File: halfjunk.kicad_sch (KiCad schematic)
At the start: 94 parts, among them SW0 SW_Push, U0 ATmega32U4-A

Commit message: A lot of progress on schematic
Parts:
- removed C?: 10uf, symbol Device:C_Small
- removed C? (x3): .1uF, symbol Device:C_Small
- removed D? (x40): D_Small, symbol Device:D_Small
- removed SW? (x40): SW_Push, symbol Switch:SW_Push
- added C? (x3): .1uF, symbol Device:C_Small
- added C?: 10uf, symbol Device:C_Small
- added D? (x45): D_Small, symbol Device:D_Small
- added D?: PRTR5V0U2X, Package_TO_SOT_SMD:SOT-143, symbol Power_Protection:PRTR5V0U2X
- added F?: 500m, symbol Device:Polyfuse_Small
- added J?: AVR-ISP-6, symbol Connector:AVR-ISP-6
- added J? (x2): USB_C_Receptacle_USB2.0, symbol Connector:USB_C_Receptacle_USB2.0
- added R? (x2): 5.1k, symbol Device:R_Small
- added R? (x2): 4.7K, symbol Device:R_Small
- added SW? (x45): SW_Push, symbol Switch:SW_Push
- added SW?: RotaryEncoder, symbol Device:RotaryEncoder
- R?: value R_Small -> 10k
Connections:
- net +5V: now also C?.1, C?.1, C?.1, C?.1, F?.2, J?.2 (VCC), J?.A4 (VBUS), J?.A9 (VBUS), J?.B4 (VBUS), J?.B9 (VBUS)
- net D+: now also D?.2 (I/O1), J?.A6 (D+), J?.B6 (D+)
- net D-: now also D?.3 (I/O2), J?.A7 (D-), J?.B7 (D-)
- net GND: now also C?.2, C?.2, C?.2, C?.2, D?.1 (GND), J?.6 (GND), J?.A1 (GND), J?.A1 (GND), J?.A12 (GND), J?.A12 (GND), J?.B1 (GND), J?.B1 (GND), J?.B12 (GND), J?.B12 (GND), J?.S1 (SHIELD), J?.S1 (SHIELD), R?.2, R?.2, SW?.C
- net RST: now reaches R?.2, SW0.2, U0.13 (~{RESET})
- net RST: now also J?.5 (~{RST})
- net MOSI: now reaches U0.10 (PB2)
- net MOSI: now also J?.4 (MOSI)
- net MISO: now reaches U0.11 (PB3)
- net MISO: now also J?.1 (MISO)
- net ENC_A: now reaches U0.18 (PD0)
- net ENC_A: now also SW?.A
- net ENC_B: now reaches U0.19 (PD1)
- net ENC_B: now also SW?.B
- net at U0.20 (PD2): now also R?.1
- net at U0.21 (PD3): now also R?.1
- net ROW_0: now reaches U0.22 (PD5)
- net ROW_0: now also D?.1 (K), D?.1 (K), D?.1 (K), D?.1 (K), D?.1 (K), D?.1 (K), D?.1 (K)
- net ROW_1: now reaches U0.25 (PD4)
- net ROW_1: now also D?.1 (K), D?.1 (K), D?.1 (K), D?.1 (K), D?.1 (K), D?.1 (K), D?.1 (K)
- net ROW_2: now reaches U0.26 (PD6)
- net ROW_2: now also D?.1 (K), D?.1 (K), D?.1 (K), D?.1 (K), D?.1 (K), D?.1 (K), D?.1 (K)
- net ROW_3: now reaches U0.27 (PD7)
- net ROW_3: now also D?.1 (K), D?.1 (K), D?.1 (K), D?.1 (K), D?.1 (K), D?.1 (K), D?.1 (K)
- net ROW_4: now reaches U0.28 (PB4)
- net ROW_4: now also D?.1 (K), D?.1 (K), D?.1 (K), D?.1 (K), D?.1 (K), D?.1 (K), D?.1 (K)
- net ROW_5: now reaches U0.29 (PB5)
- net ROW_5: now also D?.1 (K), D?.1 (K), D?.1 (K), D?.1 (K), D?.1 (K)
- net ROW_6: now reaches U0.30 (PB6)
- net ROW_6: now also D?.1 (K), D?.1 (K), D?.1 (K), D?.1 (K), D?.1 (K)
- net COL_5: now reaches U0.36 (PF7)
- net COL_5: now also SW?.2, SW?.2, SW?.2, SW?.2, SW?.2, SW?.2, SW?.2
- net COL_4: now reaches U0.37 (PF6)
- net COL_4: now also SW?.2, SW?.2, SW?.2, SW?.2, SW?.2, SW?.2, SW?.2
- net COL_3: now reaches U0.38 (PF5)
- net COL_3: now also SW?.2, SW?.2, SW?.2, SW?.2, SW?.2, SW?.2, SW?.2
- net COL_2: now reaches U0.39 (PF4)
- net COL_2: now also SW?.2, SW?.2, SW?.2, SW?.2, SW?.2, SW?.2, SW?.2
- net COL_1: now reaches U0.40 (PF1)
- net COL_1: now also SW?.2, SW?.2, SW?.2, SW?.2, SW?.2
- net COL_0: now reaches U0.41 (PF0)
- net COL_0: now also SW?.2, SW?.2, SW?.2, SW?.2, SW?.2
- net SCLK: now reaches U0.9 (PB1)
- net SCLK: now also J?.3 (SCK)
- new net: D?.2 (A), SW?.1 (x45)
- new net: J?.B5 (CC2), R?.1
- new net: J?.A5 (CC1), R?.1
- new net COL_6: SW?.2, SW?.2, SW?.2, SW?.2, SW?.2, SW?.2, SW?.2
- new net DATA_1: J?.A7 (D-), J?.B7 (D-), R?.2
- new net DATA_2: J?.A6 (D+), J?.B6 (D+), R?.2
- new net VCC: D?.4 (VCC), F?.1, J?.A4 (VBUS), J?.A9 (VBUS), J?.B4 (VBUS), J?.B9 (VBUS)
- no-connect marks 0 -> 3
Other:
- note added: "Decoupling Capacitors"
- note added: "ISP"
- note added: "MCU"
- note added: "Scroll Drum"
- note added: "USB-C PC"
- moved on the sheet: C?, R?, SW0, U0, Y?

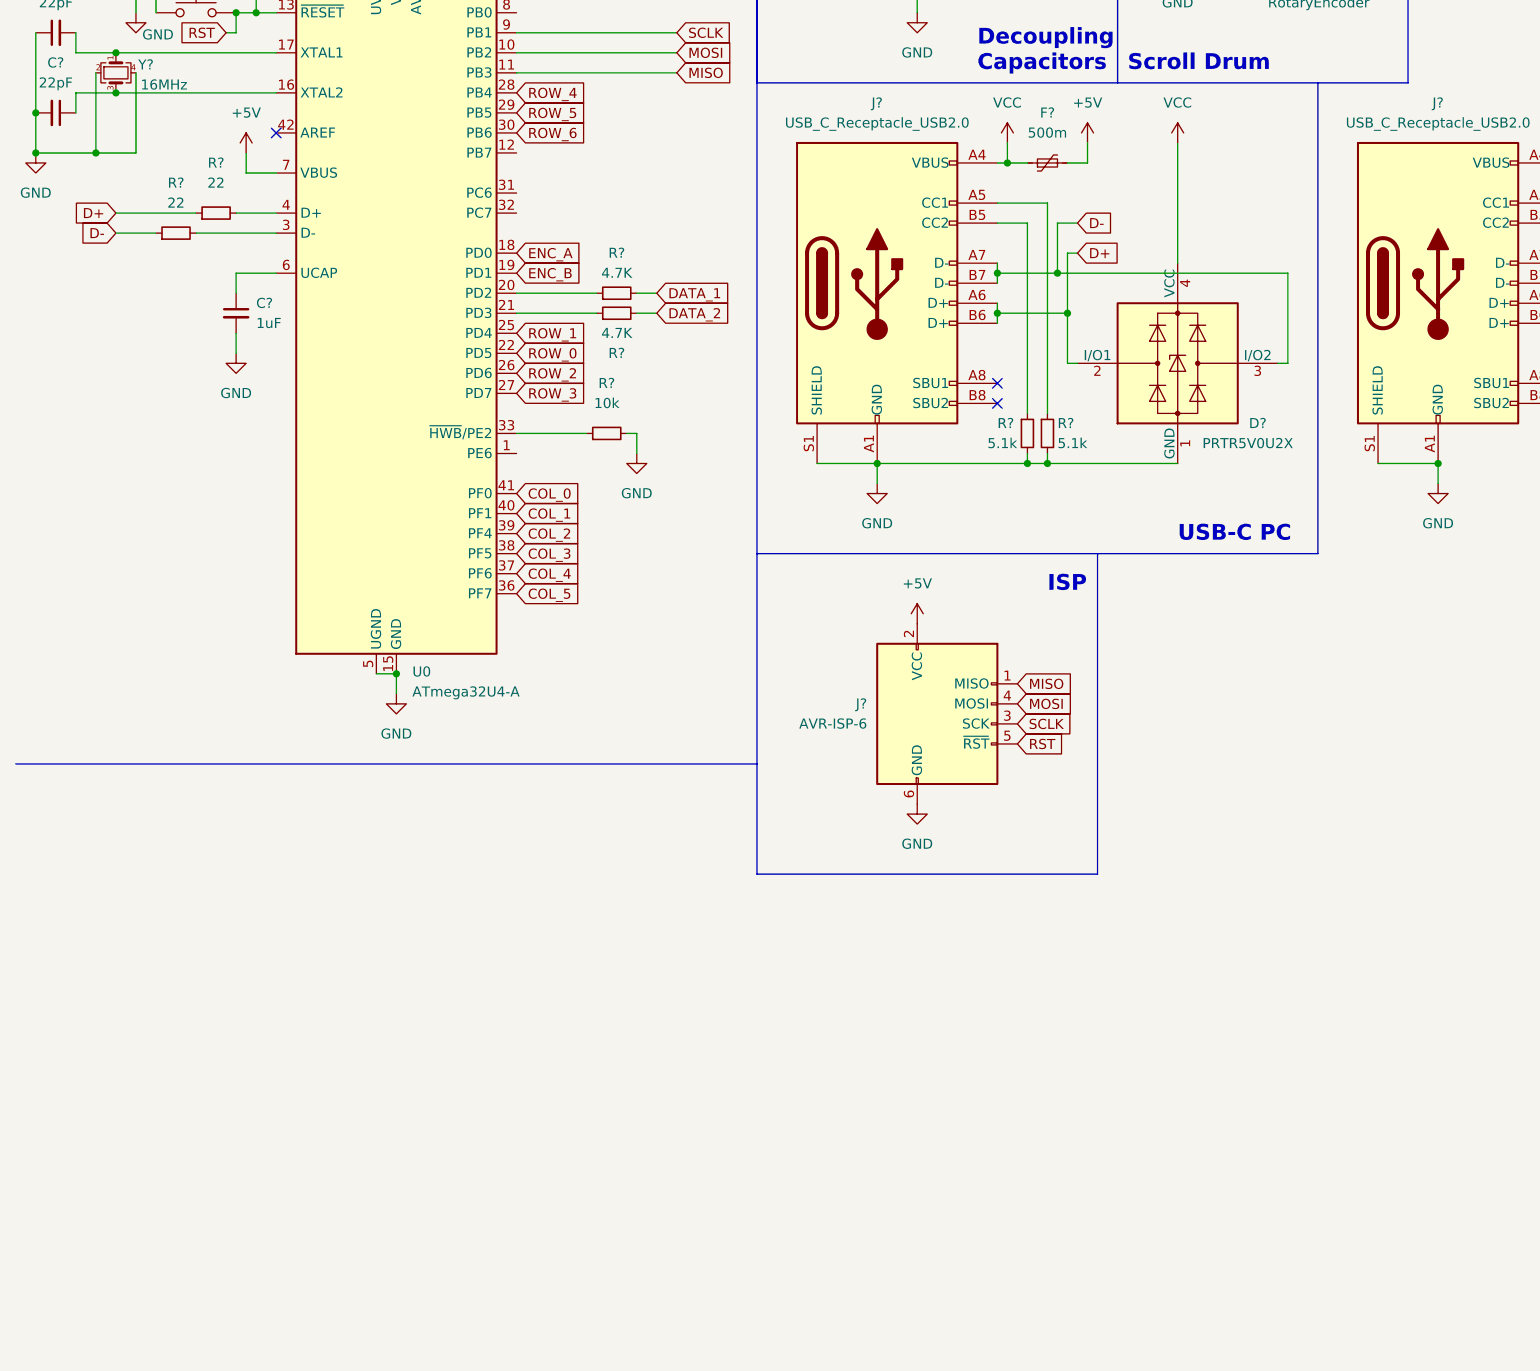
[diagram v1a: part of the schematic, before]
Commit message: added LEDs
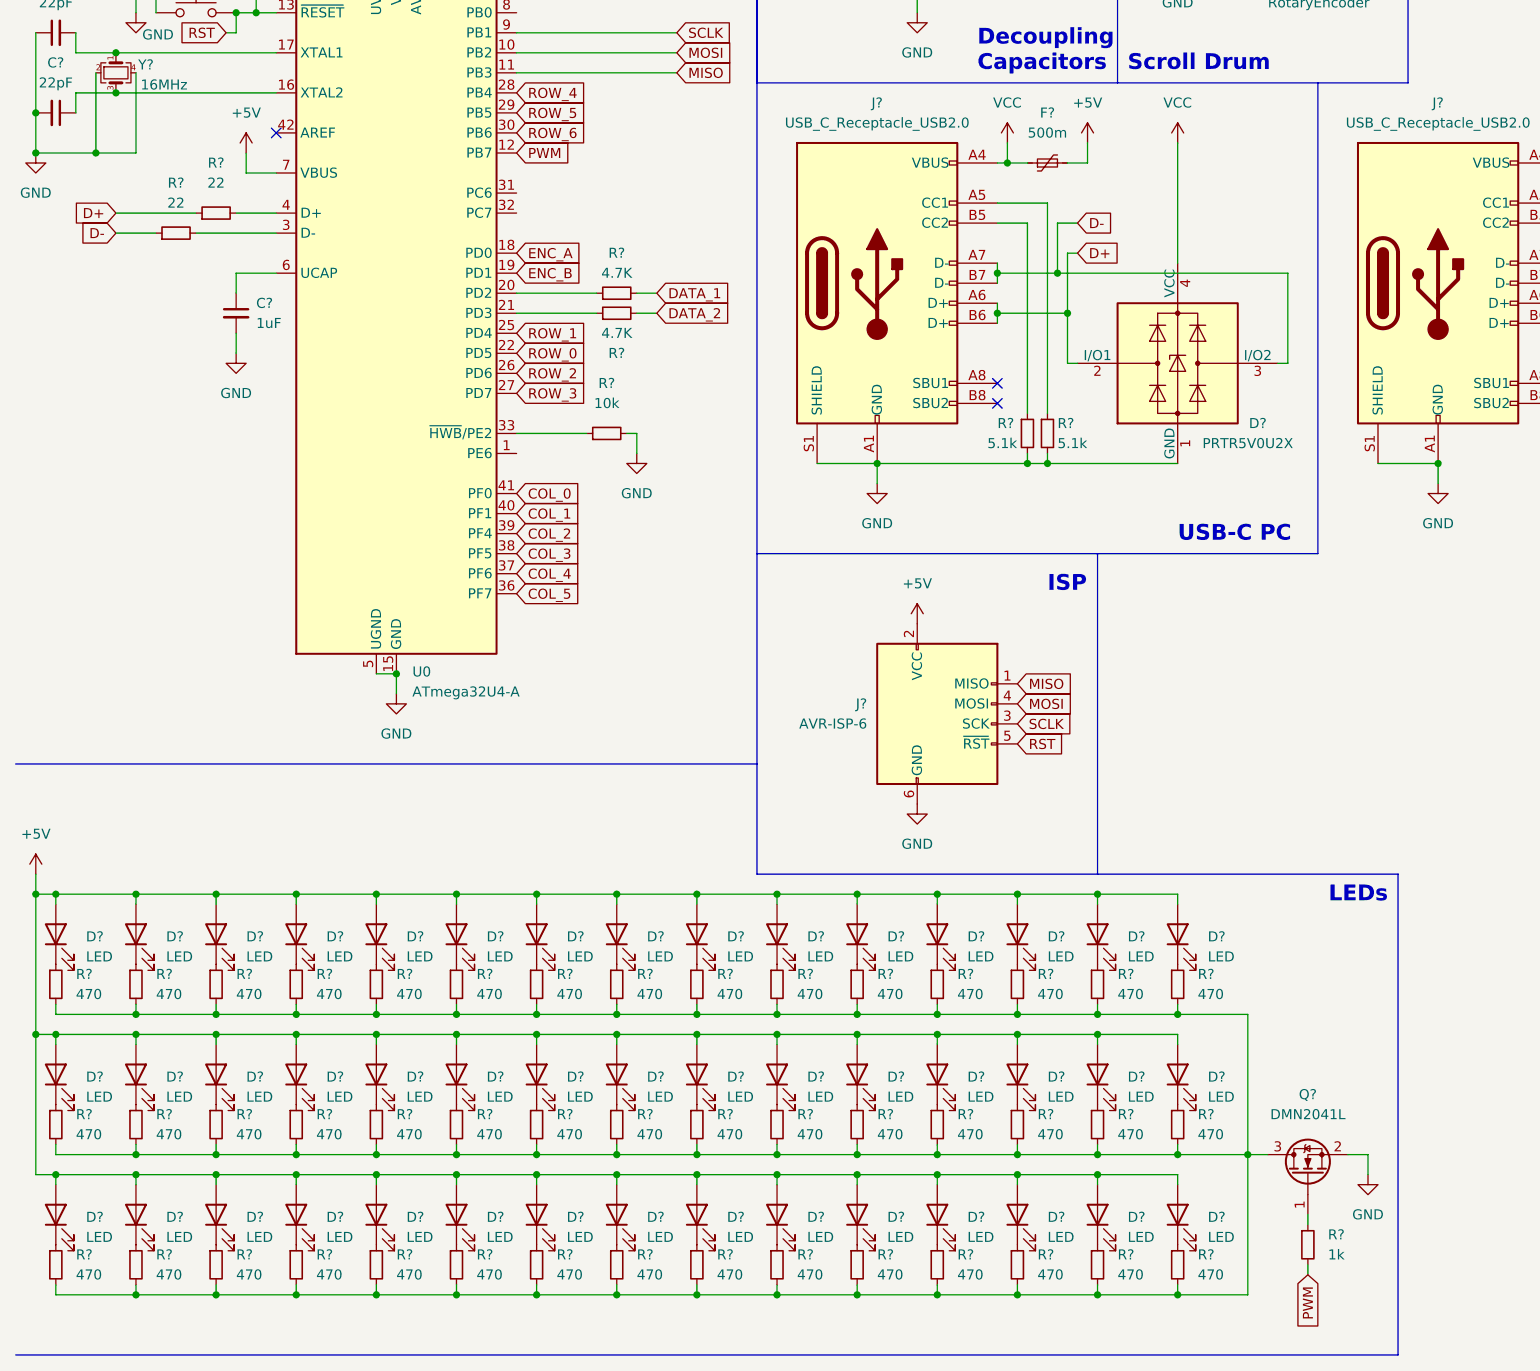
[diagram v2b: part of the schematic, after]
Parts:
- added D? (x45): LED, symbol Device:LED
- added Q?: DMN2041L, Package_TO_SOT_SMD:SOT-23, symbol Transistor_FET:DMN2041L
- added R? (x45): 470, symbol Device:R_Small
- added R?: 1k, symbol Device:R_Small
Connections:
- net +5V: now also D?.2 (A), D?.2 (A), D?.2 (A), D?.2 (A), D?.2 (A), D?.2 (A), D?.2 (A), D?.2 (A), D?.2 (A), D?.2 (A), D?.2 (A), D?.2 (A), D?.2 (A), D?.2 (A), D?.2 (A), D?.2 (A), D?.2 (A), D?.2 (A), D?.2 (A), D?.2 (A), D?.2 (A), D?.2 (A), D?.2 (A), D?.2 (A), D?.2 (A), D?.2 (A), D?.2 (A), D?.2 (A), D?.2 (A), D?.2 (A), D?.2 (A), D?.2 (A), D?.2 (A), D?.2 (A), D?.2 (A), D?.2 (A), D?.2 (A), D?.2 (A), D?.2 (A), D?.2 (A), D?.2 (A), D?.2 (A), D?.2 (A), D?.2 (A), D?.2 (A)
- net GND: now also Q?.2 (S)
- net PWM: now reaches U0.12 (PB7)
- net PWM: now also R?.2
- new net: D?.1 (K), R?.1 (x45)
- new net: Q?.3 (D), R?.2, R?.2, R?.2, R?.2, R?.2, R?.2, R?.2, R?.2, R?.2, R?.2, R?.2, R?.2, R?.2, R?.2, R?.2, R?.2, R?.2, R?.2, R?.2, R?.2, R?.2, R?.2, R?.2, R?.2, R?.2, R?.2, R?.2, R?.2, R?.2, R?.2, R?.2, R?.2, R?.2, R?.2, R?.2, R?.2, R?.2, R?.2, R?.2, R?.2, R?.2, R?.2, R?.2, R?.2, R?.2
- new net: Q?.1 (G), R?.1
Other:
- note added: "LEDs"

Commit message: Split sch into two sheets for left and right
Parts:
- removed C? (x3): .1uF, symbol Device:C_Small
- removed C? (x2): 22pF, symbol Device:C_Small
- removed C?: 1uF, symbol Device:C_Small
- removed C?: 10uf, symbol Device:C_Small
- removed D? (x45): D_Small, symbol Device:D_Small
- removed D? (x45): LED, symbol Device:LED
- removed D?: PRTR5V0U2X, Package_TO_SOT_SMD:SOT-143, symbol Power_Protection:PRTR5V0U2X
- removed F?: 500m, symbol Device:Polyfuse_Small
- removed J?: AVR-ISP-6, symbol Connector:AVR-ISP-6
- removed J? (x2): USB_C_Receptacle_USB2.0, symbol Connector:USB_C_Receptacle_USB2.0
- removed Q?: DMN2041L, Package_TO_SOT_SMD:SOT-23, symbol Transistor_FET:DMN2041L
- removed R? (x45): 470, symbol Device:R_Small
- removed R? (x2): 5.1k, symbol Device:R_Small
- removed R? (x2): 4.7K, symbol Device:R_Small
- removed R? (x2): 10k, symbol Device:R_Small
- removed R? (x2): 22, symbol Device:R_Small
- removed R?: 1k, symbol Device:R_Small
- removed SW0: SW_Push, Button_Switch_SMD:SW_SPST_SKQG_WithStem, symbol Switch:SW_Push
- removed SW? (x45): SW_Push, symbol Switch:SW_Push
- removed SW?: RotaryEncoder, symbol Device:RotaryEncoder
- removed U0: ATmega32U4-A, ATmega32U4:ATmega32U4, symbol MCU_Microchip_ATmega:ATmega32U4-A
- removed Y?: 16MHz, symbol Device:Crystal_GND24_Small
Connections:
- no-connect marks 3 -> 0
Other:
- added sheet Left (Left.kicad_sch)
- added sheet Right (Right.kicad_sch)
- note removed: "Decoupling Capacitors"
- note removed: "ISP"
- note removed: "LEDs"
- note removed: "MCU"
- note removed: "Scroll Drum"
- note removed: "USB-C PC"

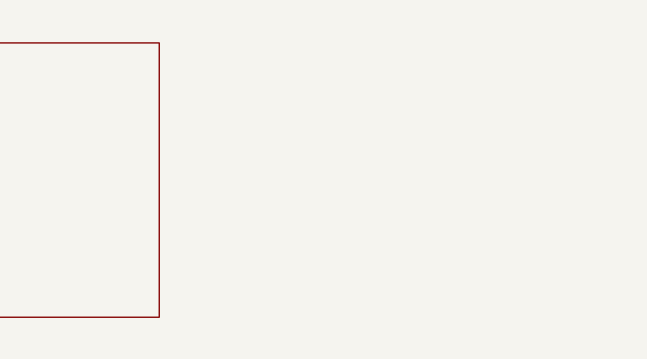
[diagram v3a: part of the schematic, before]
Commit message: added a numpad
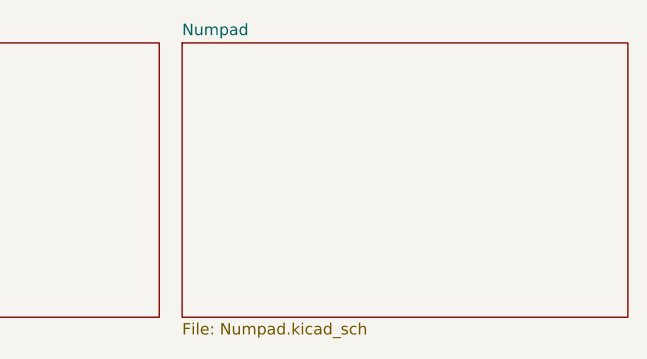
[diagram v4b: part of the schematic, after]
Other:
- added sheet Numpad (Numpad.kicad_sch)

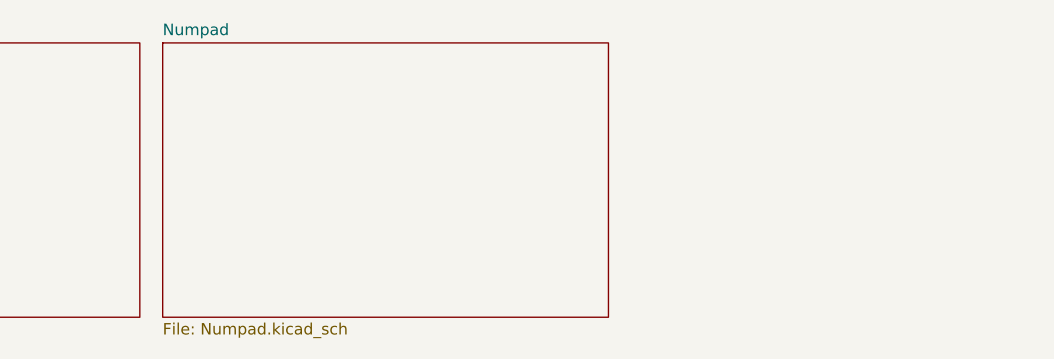
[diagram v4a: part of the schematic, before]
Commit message: replaced LEDs with RGBs, and started the PCB for keyboard
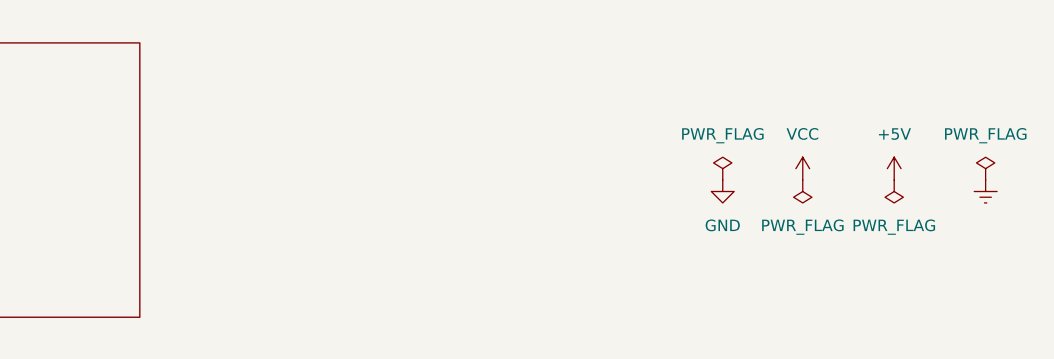
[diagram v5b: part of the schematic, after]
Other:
- removed sheet Numpad
